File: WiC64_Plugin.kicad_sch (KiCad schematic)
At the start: 62 parts, among them CN1 USERPORT-C64, Q1 BSS138, Q10 BSS138, Q11 BSS138, Q2 BSS138, Q3 BSS138, Q4 BSS138, Q5 BSS138, Q6 BSS138, Q7 BSS138, Q8 BSS138, Q9 BSS138, SW1 RESET-C64, SW2 Function

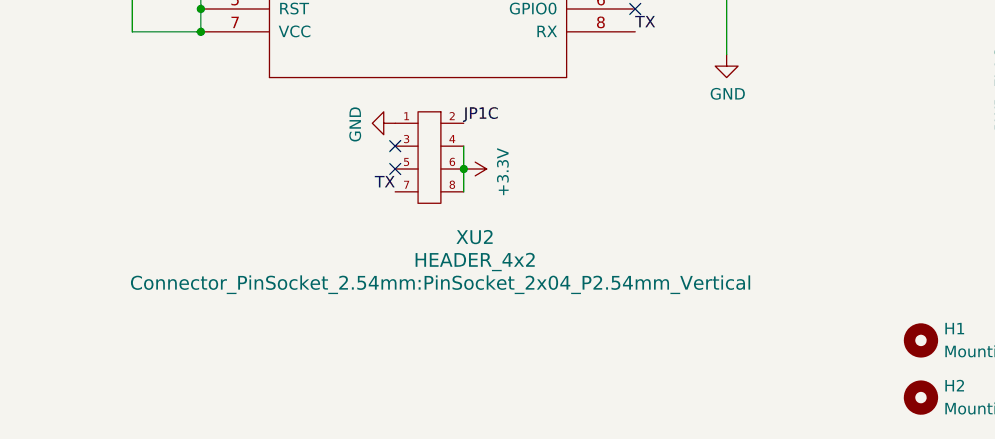
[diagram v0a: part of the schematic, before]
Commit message: Make all resistors 0805
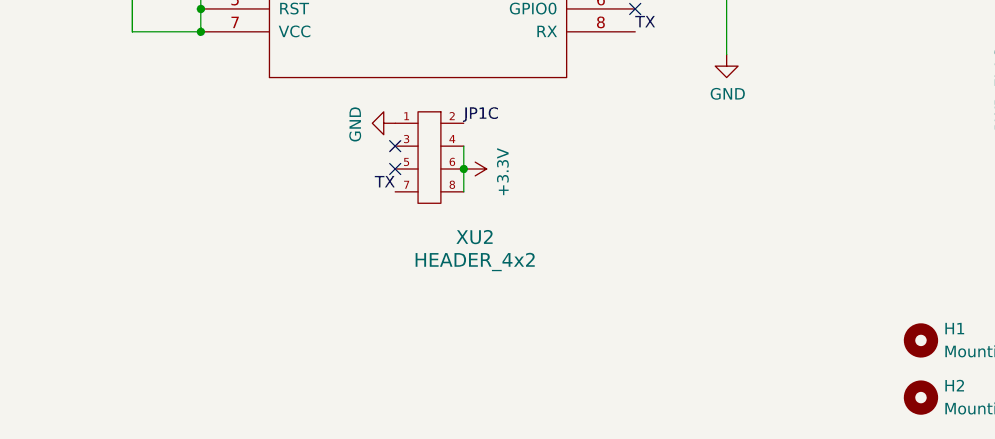
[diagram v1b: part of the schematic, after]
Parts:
- R1, R10, R11, R12, R13, R14, R15, R16, R17, R18, R19, R2, R20, R21, R22, R23, R24, R25, R26, R3, R4, R5, R6, R7, R8, R9: footprint Resistor_SMD:R_0603_1608Metric -> Resistor_SMD:R_0805_2012Metric_Pad1.20x1.40mm_HandSolder
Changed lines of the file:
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@@
 			)
 		)
-		(property "Footprint" "Resistor_SMD:R_0603_1608Metric"
+		(property "Footprint" "Resistor_SMD:R_0805_2012Metric_Pad1.20x1.40mm_HandSolder"
 			(at 31.242 31.75 90)
 			(effects
@@
 			)
 		)
-		(property "Footprint" "Resistor_SMD:R_0603_1608Metric"
+		(property "Footprint" "Resistor_SMD:R_0805_2012Metric_Pad1.20x1.40mm_HandSolder"
 			(at 43.942 31.75 90)
 			(effects
@@
 			)
 		)
-		(property "Footprint" "Resistor_SMD:R_0603_1608Metric"
+		(property "Footprint" "Resistor_SMD:R_0805_2012Metric_Pad1.20x1.40mm_HandSolder"
 			(at 52.832 31.75 90)
 			(effects
@@
 			)
 		)
-		(property "Footprint" "Resistor_SMD:R_0603_1608Metric"
+		(property "Footprint" "Resistor_SMD:R_0805_2012Metric_Pad1.20x1.40mm_HandSolder"
 			(at 65.532 31.75 90)
 			(effects
@@
 			)
 		)
-		(property "Footprint" "Resistor_SMD:R_0603_1608Metric"
+		(property "Footprint" "Resistor_SMD:R_0805_2012Metric_Pad1.20x1.40mm_HandSolder"
 			(at 74.422 31.75 90)
 			(effects
@@
 			)
 		)
-		(property "Footprint" "Resistor_SMD:R_0603_1608Metric"
+		(property "Footprint" "Resistor_SMD:R_0805_2012Metric_Pad1.20x1.40mm_HandSolder"
 			(at 87.122 31.75 90)
 			(effects
@@
 			)
 		)
-		(property "Footprint" "Resistor_SMD:R_0603_1608Metric"
+		(property "Footprint" "Resistor_SMD:R_0805_2012Metric_Pad1.20x1.40mm_HandSolder"
 			(at 96.012 31.75 90)
 			(effects
@@
 			)
 		)
-		(property "Footprint" "Resistor_SMD:R_0603_1608Metric"
+		(property "Footprint" "Resistor_SMD:R_0805_2012Metric_Pad1.20x1.40mm_HandSolder"
 			(at 108.712 31.75 90)
 			(effects
@@
 			)
 		)
-		(property "Footprint" "Resistor_SMD:R_0603_1608Metric"
+		(property "Footprint" "Resistor_SMD:R_0805_2012Metric_Pad1.20x1.40mm_HandSolder"
 			(at 117.602 31.75 90)
 			(effects
@@
 			)
 		)
-		(property "Footprint" "Resistor_SMD:R_0603_1608Metric"
+		(property "Footprint" "Resistor_SMD:R_0805_2012Metric_Pad1.20x1.40mm_HandSolder"
 			(at 130.302 31.75 90)
 			(effects
@@
 			)
 		)
-		(property "Footprint" "Resistor_SMD:R_0603_1608Metric"
+		(property "Footprint" "Resistor_SMD:R_0805_2012Metric_Pad1.20x1.40mm_HandSolder"
 			(at 139.192 31.75 90)
 			(effects
@@
 			)
 		)
-		(property "Footprint" "Resistor_SMD:R_0603_1608Metric"
+		(property "Footprint" "Resistor_SMD:R_0805_2012Metric_Pad1.20x1.40mm_HandSolder"
 			(at 151.892 31.75 90)
 			(effects
@@
 			)
 		)
-		(property "Footprint" "Resistor_SMD:R_0603_1608Metric"
+		(property "Footprint" "Resistor_SMD:R_0805_2012Metric_Pad1.20x1.40mm_HandSolder"
 			(at 160.782 31.75 90)
 			(effects
@@
 			)
 		)
-		(property "Footprint" "Resistor_SMD:R_0603_1608Metric"
+		(property "Footprint" "Resistor_SMD:R_0805_2012Metric_Pad1.20x1.40mm_HandSolder"
 			(at 173.482 31.75 90)
 			(effects
@@
 			)
 		)
-		(property "Footprint" "Resistor_SMD:R_0603_1608Metric"
+		(property "Footprint" "Resistor_SMD:R_0805_2012Metric_Pad1.20x1.40mm_HandSolder"
 			(at 182.372 31.75 90)
 			(effects
@@
 			)
 		)
-		(property "Footprint" "Resistor_SMD:R_0603_1608Metric"
+		(property "Footprint" "Resistor_SMD:R_0805_2012Metric_Pad1.20x1.40mm_HandSolder"
 			(at 195.072 31.75 90)
 			(effects
@@
 			)
 		)
-		(property "Footprint" "Resistor_SMD:R_0603_1608Metric"
+		(property "Footprint" "Resistor_SMD:R_0805_2012Metric_Pad1.20x1.40mm_HandSolder"
 			(at 203.962 31.75 90)
 			(effects
@@
 			)
 		)
-		(property "Footprint" "Resistor_SMD:R_0603_1608Metric"
+		(property "Footprint" "Resistor_SMD:R_0805_2012Metric_Pad1.20x1.40mm_HandSolder"
 			(at 216.662 31.75 90)
 			(effects
@@
 			)
 		)
-		(property "Footprint" "Resistor_SMD:R_0603_1608Metric"
+		(property "Footprint" "Resistor_SMD:R_0805_2012Metric_Pad1.20x1.40mm_HandSolder"
 			(at 225.552 31.75 90)
 			(effects
@@
 			)
 		)
-		(property "Footprint" "Resistor_SMD:R_0603_1608Metric"
+		(property "Footprint" "Resistor_SMD:R_0805_2012Metric_Pad1.20x1.40mm_HandSolder"
 			(at 238.252 31.75 90)
 			(effects
@@
 			)
 		)
-		(property "Footprint" "Resistor_SMD:R_0603_1608Metric"
+		(property "Footprint" "Resistor_SMD:R_0805_2012Metric_Pad1.20x1.40mm_HandSolder"
 			(at 247.142 31.75 90)
 			(effects
@@
 			)
 		)
-		(property "Footprint" "Resistor_SMD:R_0603_1608Metric"
+		(property "Footprint" "Resistor_SMD:R_0805_2012Metric_Pad1.20x1.40mm_HandSolder"
 			(at 259.842 31.75 90)
 			(effects
@@
 			)
 		)
-		(property "Footprint" "Resistor_SMD:R_0603_1608Metric"
+		(property "Footprint" "Resistor_SMD:R_0805_2012Metric_Pad1.20x1.40mm_HandSolder"
 			(at 37.592 67.31 90)
 			(effects
@@
 			)
 		)
-		(property "Footprint" "Resistor_SMD:R_0603_1608Metric"
+		(property "Footprint" "Resistor_SMD:R_0805_2012Metric_Pad1.20x1.40mm_HandSolder"
 			(at 33.782 67.31 90)
 			(effects
@@
 			)
 		)
-		(property "Footprint" "Resistor_SMD:R_0603_1608Metric"
+		(property "Footprint" "Resistor_SMD:R_0805_2012Metric_Pad1.20x1.40mm_HandSolder"
 			(at 263.652 134.62 90)
 			(effects
@@
 			)
 		)
-		(property "Footprint" "Resistor_SMD:R_0603_1608Metric"
+		(property "Footprint" "Resistor_SMD:R_0805_2012Metric_Pad1.20x1.40mm_HandSolder"
 			(at 45.212 67.31 90)
 			(effects
@@
 					(size 1.524 1.524)
 				)
+				(hide yes)
 			)
 		)

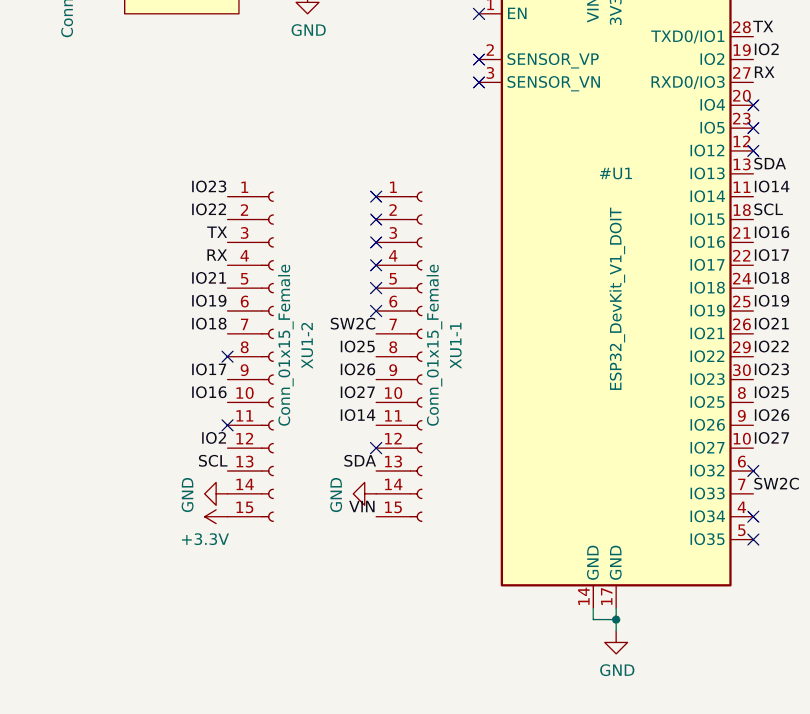
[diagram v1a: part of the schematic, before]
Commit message: Add 3D models
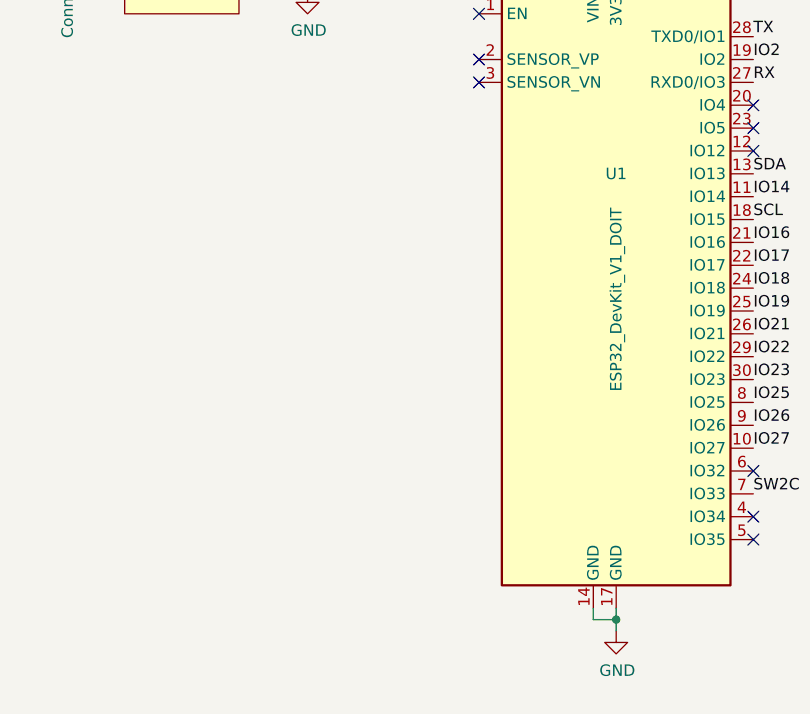
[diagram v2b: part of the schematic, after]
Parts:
- removed XU1-1, XU1-2: Conn_01x15_Female, w_pin_strip:pin_socket_15, symbol Connector:Conn_01x15_Socket
- U1: renamed from #U1; footprint ESP32_DevKit_V1_DOIT:esp32_devkit_v1_doit -> WiC64:esp32_devkit_v1_doit
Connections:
- no-connect marks 27 -> 18

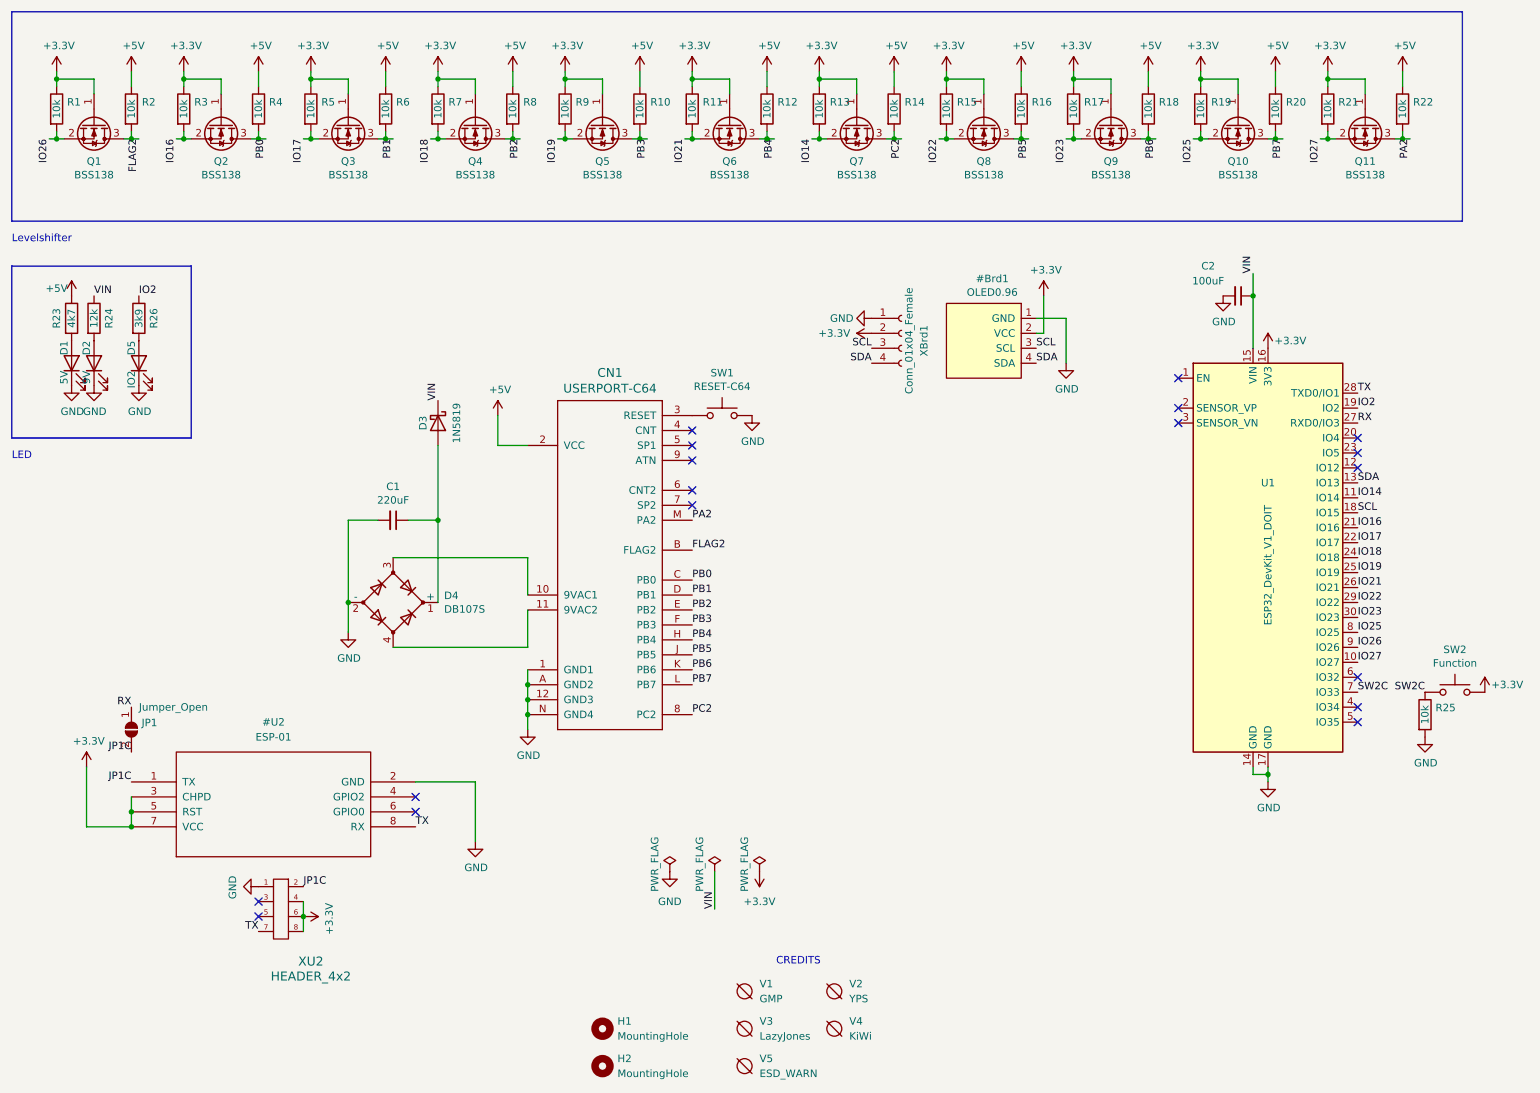
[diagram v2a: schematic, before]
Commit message: Remove redundant symbols
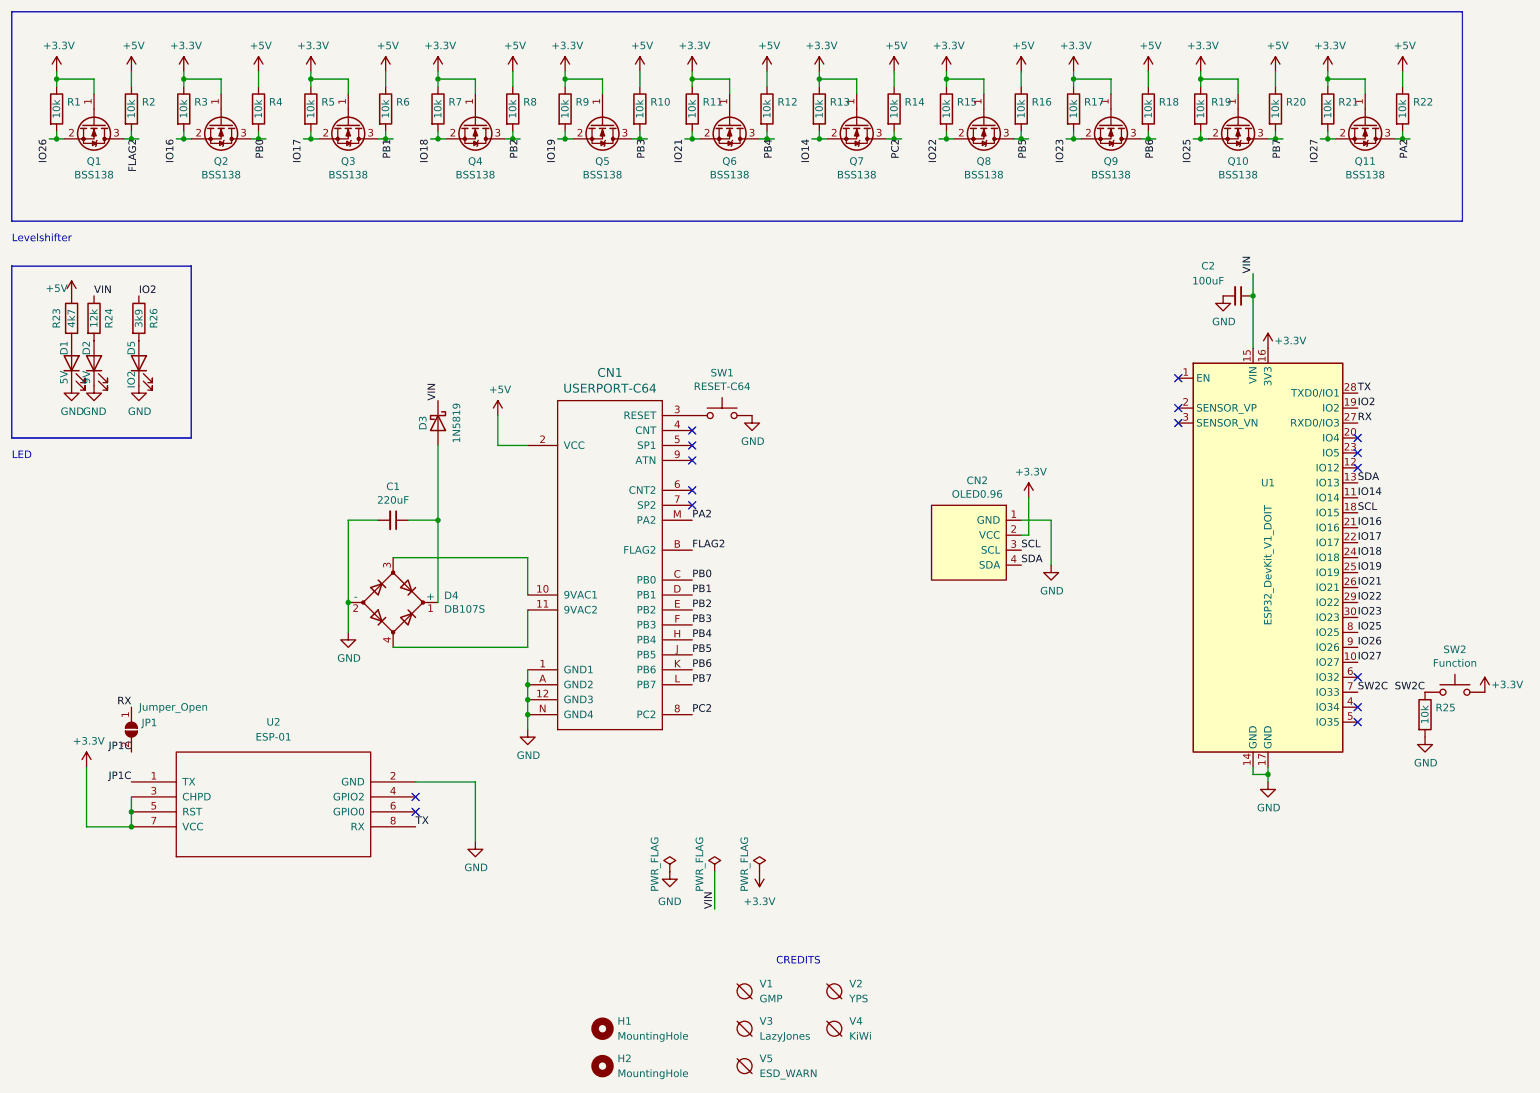
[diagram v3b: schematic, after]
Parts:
- removed XBrd1: Conn_01x04_Female, Connector_PinSocket_2.54mm:PinSocket_1x04_P2.54mm_Vertical, symbol Connector:Conn_01x04_Socket
- removed XU2: HEADER_4x2, Connector_PinSocket_2.54mm:PinSocket_2x04_P2.54mm_Vertical, symbol w_connectors:HEADER_4x2
- CN2: renamed from #Brd1; footprint SSD1306-128x64_OLED:SSD1306-128x64_OLED -> Connector_PinSocket_2.54mm:PinSocket_1x04_P2.54mm_Vertical
- U2: renamed from #U2; footprint ESP8266:ESP-01 -> WiC64:ESP-01
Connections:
- no-connect marks 18 -> 16

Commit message: Allow powering ESP32 from 5V
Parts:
- added JP2: JMP_ESP_POWER, Jumper:SolderJumper-3_P1.3mm_Open_RoundedPad1.0x1.5mm, symbol Jumper:Jumper_3_Open
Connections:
- net +5V: now also JP2.1 (A)
- net VIN: no longer C2.1, D3.1 (K), R24.1, U1.15 (VIN)
- net at C1.1, D4.1 (+): now also JP2.3 (B); no longer D3.2 (A)
- new net: D3.2 (A), JP2.2 (C)
- new net VCC: C2.1, D3.1 (K), R24.1, U1.15 (VIN)
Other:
- note added: "ESP32 DEVKIT POWER"
- note added: "VIN range: 4.5-12V"
- moved on the sheet: C1, D3, D4

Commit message: Move all footprints to single library
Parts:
- CN1: footprint cbm-connectors:UPS24CONN -> WiC64:UPS24CONN
- V1: footprint Logo:GMP -> WiC64:GMP
- V2: footprint Logo:YPS2 -> WiC64:YPS2
- V3: footprint Logo:LazyJones2 -> WiC64:LazyJones2
- V4: footprint Logo:KiWi -> WiC64:KiWi
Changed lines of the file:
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@@
 			)
 		)
-		(property "Footprint" "cbm-connectors:UPS24CONN"
+		(property "Footprint" "WiC64:UPS24CONN"
 			(at 128.27 109.22 0)
 			(effects
@@
 			)
 		)
-		(property "Footprint" "Logo:LazyJones2"
+		(property "Footprint" "WiC64:LazyJones2"
 			(at 149.86 187.96 0)
 			(effects
@@
 			)
 		)
-		(property "Footprint" "Logo:YPS2"
+		(property "Footprint" "WiC64:YPS2"
 			(at 165.1 181.61 0)
 			(effects
@@
 			)
 		)
-		(property "Footprint" "Logo:KiWi"
+		(property "Footprint" "WiC64:KiWi"
 			(at 165.1 187.96 0)
 			(effects
@@
 			)
 		)
-		(property "Footprint" "Logo:GMP"
+		(property "Footprint" "WiC64:GMP"
 			(at 149.86 181.61 0)
 			(effects

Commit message: WIP
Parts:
- removed JP2: JMP_ESP_POWER, Jumper:SolderJumper-3_P1.3mm_Open_RoundedPad1.0x1.5mm, symbol Jumper:Jumper_3_Open
- added D2: 1N5819, Diode_SMD:D_SMA, symbol Device:D_Schottky
- added FB1: FERRITE, WiC64:Ferrite_D6.0mm_L10.00mm_Horizontal, symbol Device:FerriteBead
- C1: footprint w_capacitors:CP_6.3x11mm_horiz-R -> WiC64:CP_6.3x11mm_horiz-R
- C2: value 100uF -> 220uF; footprint w_capacitors:CP_6.3x11mm_horiz-R -> WiC64:CP_6.3x11mm_horiz-R
- D3: footprint Diode_SMD:D_SOD-123 -> Diode_SMD:D_SMA
- renumbered D4 to D1, D1 to LD1, D2 to LD2, D5 to LD3
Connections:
- net +5V: now also D2.2 (A), FB1.1; no longer CN1.2 (VCC)
- net VCC: now also D2.1 (K)
- net at D3.2 (A): now also C1.1, D1.1 (+)
- new net: CN1.2 (VCC), FB1.2
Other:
- moved on the sheet: D3
